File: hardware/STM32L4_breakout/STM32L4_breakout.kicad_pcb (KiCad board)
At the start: 2 copper layers, 84.8 x 91.2 mm, 67 parts, among them J1 12V IN, J10 GPIO, J11 SPI1, J12 USART1, J13 USART3, J14 UART4, J15 3.3V, J16 5V, J17 12V, J2 SWD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

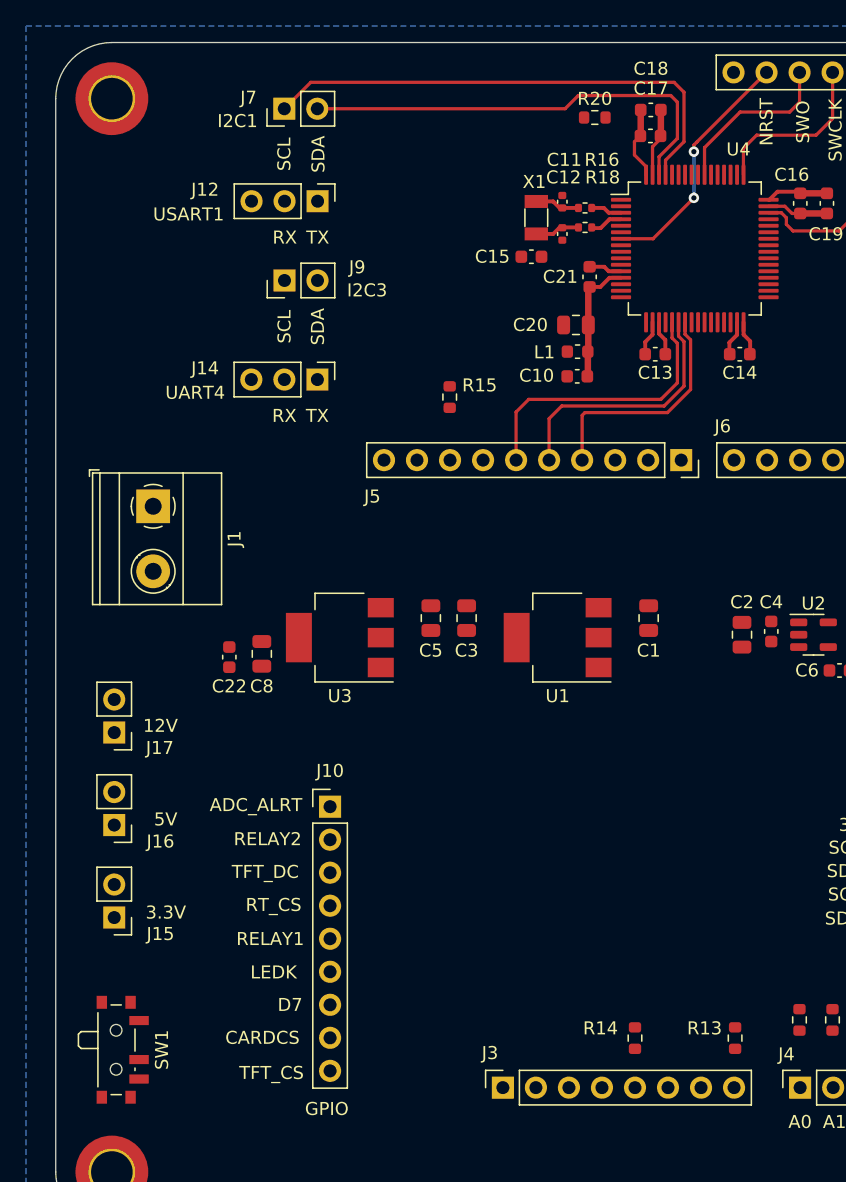
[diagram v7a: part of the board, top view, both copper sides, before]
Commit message: breakout board signal trace layout WIP
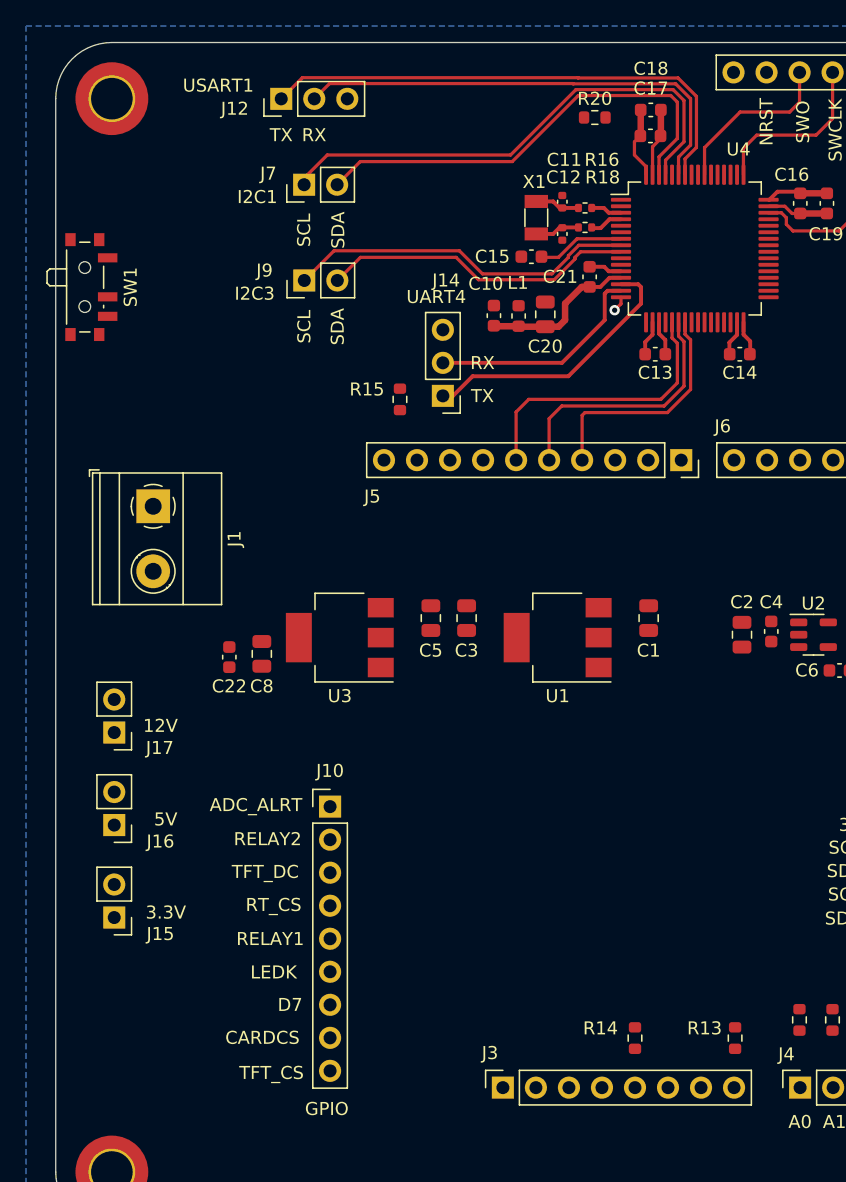
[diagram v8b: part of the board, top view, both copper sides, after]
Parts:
- moved SW1 58.7 mm to (106.4, 69.8)
- moved J14 9.73 mm to (133.6, 78.2), turned to 180 degrees
- moved J12 8.36 mm to (121.2, 55.4), turned to 90 degrees
- moved C10 7.93 mm to (137.5, 72.0), turned to 90 degrees
- moved J7 6.04 mm to (122.9, 62.0)
- moved L1 5.30 mm to (139.4, 72.1), turned to 90 degrees
- moved R15 3.83 mm to (130.3, 78.5)
- moved C20 2.50 mm to (141.5, 71.9), turned to 90 degrees
- moved J9 1.52 mm to (122.9, 69.3)
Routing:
- net USART1_TX: track 0.00 -> 39.6 mm
- net USART1_RX: track 0.00 -> 36.1 mm
- net I2C3_SCL: track 0.00 -> 27.0 mm
- net I2C3_SDA: track 0.00 -> 24.2 mm
- net UART4_TX: track 0.00 -> 21.1 mm
- net UART4_RX: track 0.00 -> 17.2 mm
- net STM_NRST: track 18.9 -> 6.73 mm, vias 2 -> 0
- net +3.3VA: track 9.65 -> 12.3 mm
- net TFT_CS: track 0.00 -> 1.20 mm, vias 0 -> 1
- net I2C1_SDA: track 34.5 -> 35.4 mm
